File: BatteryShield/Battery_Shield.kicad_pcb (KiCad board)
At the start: 2 copper layers, 95 x 123.4 mm, 66 parts, among them J100 Conn_02x02_Counter_Clockwise, J600 Conn_02x03_Counter_Clockwise, J700 MOLEX-MINIFIT-JR-5556, K100 G5LE-14 DC3, K101 G5LE-14 DC3, K200 G5LE-14 DC3, Q100 ZVP4525G, Q101 ZVP4525G, Q200 ZVP4525G, U300 LTC4151IMS-1, U301 MOCD207M, U302 MOCD207M, U400 ADC081C021, U401 LM35-D, U600 LT8608, U601 LTC3642-3.3

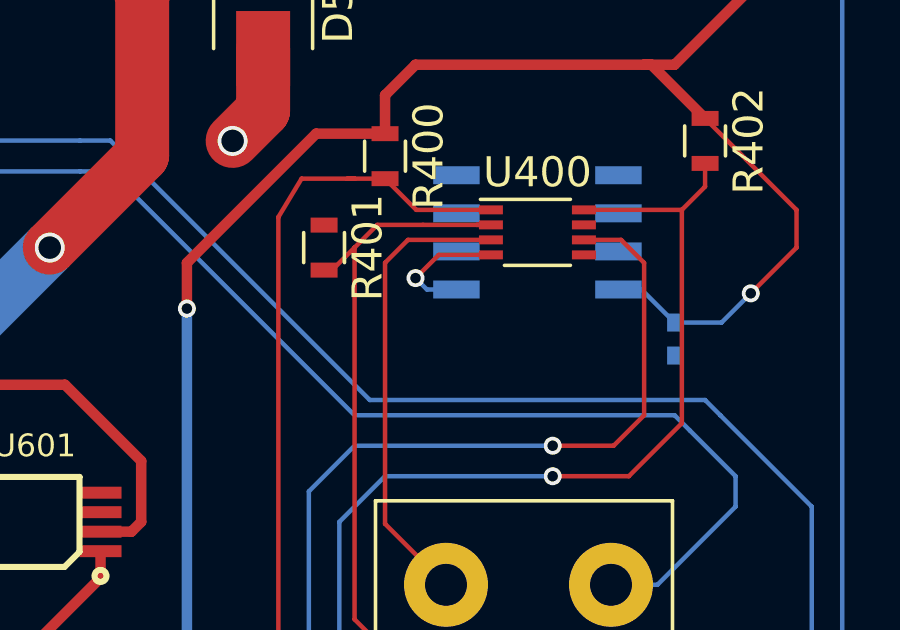
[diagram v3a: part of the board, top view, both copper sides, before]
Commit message: Added minor changes to bom/temp sensor circuit
Added small decoupling cap on temp sensor/adc input. Also added more files to the verifcation document folder
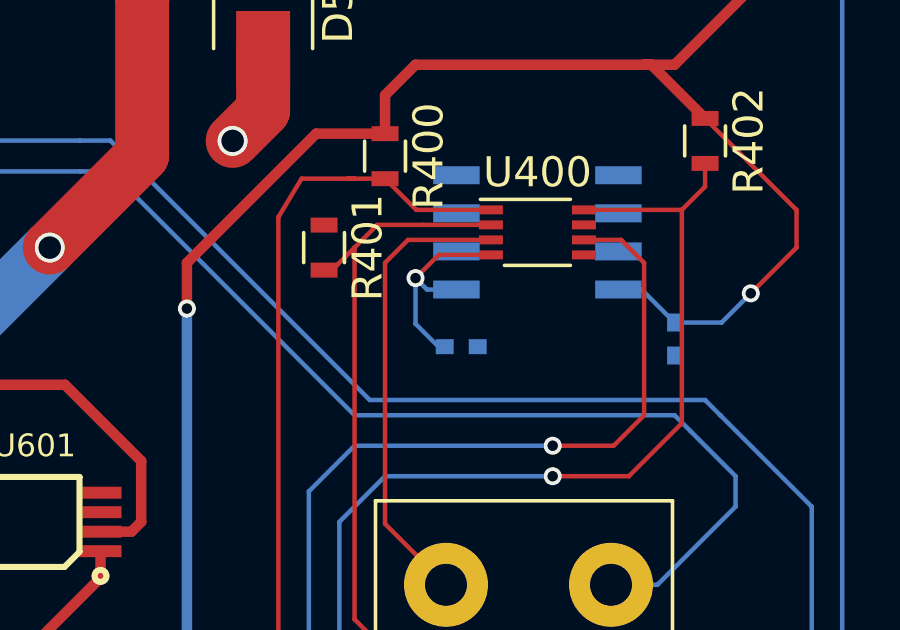
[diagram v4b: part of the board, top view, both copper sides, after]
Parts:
- added C401: 10n, Capacitors_SMD:C_0402, B.Cu at (152.4, 105.4)
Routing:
- net Net-(C401-Pad1): track 4.36 -> 7.17 mm
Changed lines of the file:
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@@
 (kicad_pcb (version 4) (host pcbnew 4.0.7)
   (general
-    (links 149)
+    (links 151)
     (no_connects 13)
     (area 81.712999 36.500999 176.859001 160.095001)
     (thickness 1.6)
     (drawings 5)
-    (tracks 581)
+    (tracks 584)
     (zones 0)
-    (modules 66)
+    (modules 67)
     (nets 53)
   )
@@
   (net 39 "Net-(U302-Pad5)")
   (net 40 "Net-(U302-Pad6)")
-  (net 41 "Net-(U400-Pad4)")
-  (net 42 "Net-(U401-Pad2)")
-  (net 43 "Net-(U401-Pad3)")
-  (net 44 "Net-(U401-Pad5)")
-  (net 45 "Net-(U401-Pad6)")
-  (net 46 "Net-(U401-Pad7)")
-  (net 47 "Net-(U601-Pad3)")
-  (net 48 "Net-(U601-Pad4)")
-  (net 49 "Net-(U601-Pad7)")
-  (net 50 "Net-(L600-Pad2)")
-  (net 51 "Net-(U600-Pad7)")
-  (net 52 "Net-(U600-Pad8)")
+  (net 41 "Net-(U401-Pad2)")
+  (net 42 "Net-(U401-Pad3)")
+  (net 43 "Net-(U401-Pad5)")
+  (net 44 "Net-(U401-Pad6)")
+  (net 45 "Net-(U401-Pad7)")
+  (net 46 "Net-(U601-Pad3)")
+  (net 47 "Net-(U601-Pad4)")
+  (net 48 "Net-(U601-Pad7)")
+  (net 49 "Net-(L600-Pad2)")
+  (net 50 "Net-(U600-Pad7)")
+  (net 51 "Net-(U600-Pad8)")
+  (net 52 "Net-(C401-Pad1)")
   (net_class Default "This is the default net class."
     (clearance 0.15)
@@
     (add_net CV_SCL_BBB)
     (add_net CV_SDA_BBB)
+    (add_net "Net-(C401-Pad1)")
     (add_net "Net-(C601-Pad1)")
     (add_net "Net-(C601-Pad2)")
@@
     (add_net "Net-(U302-Pad5)")
     (add_net "Net-(U302-Pad6)")
-    (add_net "Net-(U400-Pad4)")
     (add_net "Net-(U401-Pad2)")
     (add_net "Net-(U401-Pad3)")
@@
       (net 18 5V_REG))
     (pad 2 smd rect (at 2.44 0 90) (size 1.6 3.5) (layers F.Cu F.Paste F.Mask)
-      (net 50 "Net-(L600-Pad2)"))
+      (net 49 "Net-(L600-Pad2)"))
     (model ${KISYS3DMOD}/Inductors_SMD.3dshapes/L_1812.wrl
       (at (xyz 0 0 0))
@@
     (fp_line (start -2.075 2.525) (end -3.475 2.525) (layer B.SilkS) (width 0.15))
     (pad 1 smd rect (at -2.7 1.905) (size 1.55 0.6) (layers B.Cu B.Paste B.Mask)
-      (net 41 "Net-(U400-Pad4)"))
+      (net 52 "Net-(C401-Pad1)"))
     (pad 2 smd rect (at -2.7 0.635) (size 1.55 0.6) (layers B.Cu B.Paste B.Mask)
-      (net 42 "Net-(U401-Pad2)"))
+      (net 41 "Net-(U401-Pad2)"))
     (pad 3 smd rect (at -2.7 -0.635) (size 1.55 0.6) (layers B.Cu B.Paste B.Mask)
-      (net 43 "Net-(U401-Pad3)"))
+      (net 42 "Net-(U401-Pad3)"))
     (pad 4 smd rect (at -2.7 -1.905) (size 1.55 0.6) (layers B.Cu B.Paste B.Mask)
       (net 1 BBB_GND))
     (pad 5 smd rect (at 2.7 -1.905) (size 1.55 0.6) (layers B.Cu B.Paste B.Mask)
-      (net 44 "Net-(U401-Pad5)"))
+      (net 43 "Net-(U401-Pad5)"))
     (pad 6 smd rect (at 2.7 -0.635) (size 1.55 0.6) (layers B.Cu B.Paste B.Mask)
-      (net 45 "Net-(U401-Pad6)"))
+      (net 44 "Net-(U401-Pad6)"))
     (pad 7 smd rect (at 2.7 0.635) (size 1.55 0.6) (layers B.Cu B.Paste B.Mask)
-      (net 46 "Net-(U401-Pad7)"))
+      (net 45 "Net-(U401-Pad7)"))
     (pad 8 smd rect (at 2.7 1.905) (size 1.55 0.6) (layers B.Cu B.Paste B.Mask)
       (net 18 5V_REG))
@@
       (net 3 V_BATT37))
     (pad 3 smd rect (at -2.2 0.325 180) (size 1.4 0.4) (layers F.Cu F.Paste F.SilkS F.Mask)
-      (net 47 "Net-(U601-Pad3)"))
+      (net 46 "Net-(U601-Pad3)"))
     (pad 4 smd rect (at -2.2 0.975 180) (size 1.4 0.4) (layers F.Cu F.Paste F.SilkS F.Mask)
-      (net 48 "Net-(U601-Pad4)"))
+      (net 47 "Net-(U601-Pad4)"))
     (pad 5 smd rect (at 2.2 0.975 180) (size 1.4 0.4) (layers F.Cu F.Paste F.SilkS F.Mask)
       (net 3 V_BATT37))
@@
       (net 8 3.3V_REG))
     (pad 7 smd rect (at 2.2 -0.325 180) (size 1.4 0.4) (layers F.Cu F.Paste F.SilkS F.Mask)
-      (net 49 "Net-(U601-Pad7)"))
+      (net 48 "Net-(U601-Pad7)"))
     (pad 8 smd rect (at 2.2 -0.975 180) (size 1.4 0.4) (layers F.Cu F.Paste F.SilkS F.Mask)
       (net 1 BBB_GND))
@@
       (net 25 TEMP_SLAVE_ADDR0))
     (pad 4 smd rect (at -1.55 0.75 270) (size 0.3 0.8) (layers F.Cu F.Paste F.Mask)
-      (net 41 "Net-(U400-Pad4)"))
+      (net 52 "Net-(C401-Pad1)"))
     (pad 5 smd rect (at 1.55 0.75 270) (size 0.3 0.8) (layers F.Cu F.Paste F.Mask)
       (net 18 5V_REG))
@@
       (net 6 "Net-(C602-Pad1)"))
     (pad 2 smd rect (at -2.2 -0.5 90) (size 1.6 0.3) (layers F.Cu F.Paste F.SilkS F.Mask)
-      (net 50 "Net-(L600-Pad2)"))
+      (net 49 "Net-(L600-Pad2)"))
     (pad 3 smd rect (at -2.2 0 90) (size 1.6 0.3) (layers F.Cu F.Paste F.SilkS F.Mask)
       (net 5 "Net-(C601-Pad1)"))
@@
       (net 7 "Net-(C603-Pad2)"))
     (pad 7 smd rect (at 2.2 0.5 90) (size 1.6 0.3) (layers F.Cu F.Paste F.SilkS F.Mask)
-      (net 51 "Net-(U600-Pad7)"))
+      (net 50 "Net-(U600-Pad7)"))
     (pad 8 smd rect (at 2.2 0 90) (size 1.6 0.3) (layers F.Cu F.Paste F.SilkS F.Mask)
-      (net 52 "Net-(U600-Pad8)"))
+      (net 51 "Net-(U600-Pad8)"))
     (pad 9 smd rect (at 2.2 -0.5 90) (size 1.6 0.3) (layers F.Cu F.Paste F.SilkS F.Mask)
       (net 3 V_BATT37))
@@
       (net 1 BBB_GND))
   )
+  (module Capacitors_SMD:C_0402 (layer B.Cu)
+    (at 152.4 105.41)
+    (descr "Capacitor SMD 0402, reflow soldering, AVX (see smccp.pdf)")
+    (tags "capacitor 0402")
+    (attr smd)
+    (fp_text reference C401 (at 0 1.27) (layer B.SilkS)
+      (effects (font (size 1 1) (thickness 0.15)) (justify mirror))
+    )
+    (fp_text value 10n (at 0 -1.27) (layer B.Fab)
+      (effects (font (size 1 1) (thickness 0.15)) (justify mirror))
+    )
+    (fp_text user %R (at 0 1.27) (layer B.Fab)
+      (effects (font (size 1 1) (thickness 0.15)) (justify mirror))
+    )
+    (fp_line (start -0.5 -0.25) (end -0.5 0.25) (layer B.Fab) (width 0.1))
+    (fp_line (start 0.5 -0.25) (end -0.5 -0.25) (layer B.Fab) (width 0.1))
+    (fp_line (start 0.5 0.25) (end 0.5 -0.25) (layer B.Fab) (width 0.1))
+    (fp_line (start -0.5 0.25) (end 0.5 0.25) (layer B.Fab) (width 0.1))
+    (fp_line (start 0.25 0.47) (end -0.25 0.47) (layer B.SilkS) (width 0.12))
+    (fp_line (start -0.25 -0.47) (end 0.25 -0.47) (layer B.SilkS) (width 0.12))
+    (fp_line (start -1 0.4) (end 1 0.4) (layer B.CrtYd) (width 0.05))
+    (fp_line (start -1 0.4) (end -1 -0.4) (layer B.CrtYd) (width 0.05))
+    (fp_line (start 1 -0.4) (end 1 0.4) (layer B.CrtYd) (width 0.05))
+    (fp_line (start 1 -0.4) (end -1 -0.4) (layer B.CrtYd) (width 0.05))
+    (pad 1 smd rect (at -0.55 0) (size 0.6 0.5) (layers B.Cu B.Paste B.Mask)
+      (net 52 "Net-(C401-Pad1)"))
+    (pad 2 smd rect (at 0.55 0) (size 0.6 0.5) (layers B.Cu B.Paste B.Mask)
+      (net 1 BBB_GND))
+    (model Capacitors_SMD.3dshapes/C_0402.wrl
+      (at (xyz 0 0 0))
+      (scale (xyz 1 1 1))
+      (rotate (xyz 0 0 0))
+    )
+  )
   (gr_line (start 176.784 36.576) (end 128.524 36.576) (angle 90) (layer Edge.Cuts) (width 0.15))
   (gr_line (start 176.784 160.02) (end 176.784 36.576) (angle 90) (layer Edge.Cuts) (width 0.15))
@@
   (segment (start 125.476 112.776) (end 127.266 110.986) (width 0.15) (layer F.Cu) (net 36))
   (segment (start 127.508 110.478) (end 127.266 110.236) (width 0.15) (layer F.Cu) (net 36))
-  (segment (start 152.24 103.505) (end 151.257 103.505) (width 0.15) (layer B.Cu) (net 41))
-  (segment (start 151.65 102.35) (end 153.39 102.35) (width 0.15) (layer F.Cu) (net 41))
-  (segment (start 150.876 103.124) (end 151.65 102.35) (width 0.15) (layer F.Cu) (net 41))
-  (via (at 150.876 103.124) (size 0.6) (drill 0.35) (layers F.Cu B.Cu) (net 41))
-  (segment (start 151.257 103.505) (end 150.876 103.124) (width 0.15) (layer B.Cu) (net 41))
-  (segment (start 121.42 119.548) (end 121.42 120.488) (width 0.35) (layer F.Cu) (net 50))
-  (segment (start 121.42 120.488) (end 118.872 123.036) (width 0.35) (layer F.Cu) (net 50))
-  (segment (start 122.42 114.308) (end 122.42 115.148) (width 0.15) (layer F.Cu) (net 51) (status 20))
-  (segment (start 122.42 115.656) (end 122.42 115.324) (width 0.15) (layer F.Cu) (net 51) (status 30))
-  (segment (start 121.92 115.656) (end 121.92 115.316) (width 0.15) (layer F.Cu) (net 52) (status 30))
+  (segment (start 121.42 119.548) (end 121.42 120.488) (width 0.35) (layer F.Cu) (net 49))
+  (segment (start 121.42 120.488) (end 118.872 123.036) (width 0.35) (layer F.Cu) (net 49))
+  (segment (start 122.42 114.308) (end 122.42 115.148) (width 0.15) (layer F.Cu) (net 50) (status 20))
+  (segment (start 122.42 115.656) (end 122.42 115.324) (width 0.15) (layer F.Cu) (net 50) (status 30))
+  (segment (start 121.92 115.656) (end 121.92 115.316) (width 0.15) (layer F.Cu) (net 51) (status 30))
+  (segment (start 151.85 105.41) (end 151.638 105.41) (width 0.15) (layer B.Cu) (net 52) (status C00000))
+  (segment (start 151.638 105.41) (end 150.876 104.648) (width 0.15) (layer B.Cu) (net 52) (status 400000))
+  (segment (start 150.876 104.648) (end 150.876 103.124) (width 0.15) (layer B.Cu) (net 52))
+  (segment (start 152.24 103.505) (end 151.257 103.505) (width 0.15) (layer B.Cu) (net 52))
+  (segment (start 151.65 102.35) (end 153.39 102.35) (width 0.15) (layer F.Cu) (net 52))
+  (segment (start 150.876 103.124) (end 151.65 102.35) (width 0.15) (layer F.Cu) (net 52))
+  (via (at 150.876 103.124) (size 0.6) (drill 0.35) (layers F.Cu B.Cu) (net 52))
+  (segment (start 151.257 103.505) (end 150.876 103.124) (width 0.15) (layer B.Cu) (net 52))
   (zone (net 1) (net_name BBB_GND) (layer B.Cu) (hatch edge 0.508)
     (connect_pads (clearance 0.508))

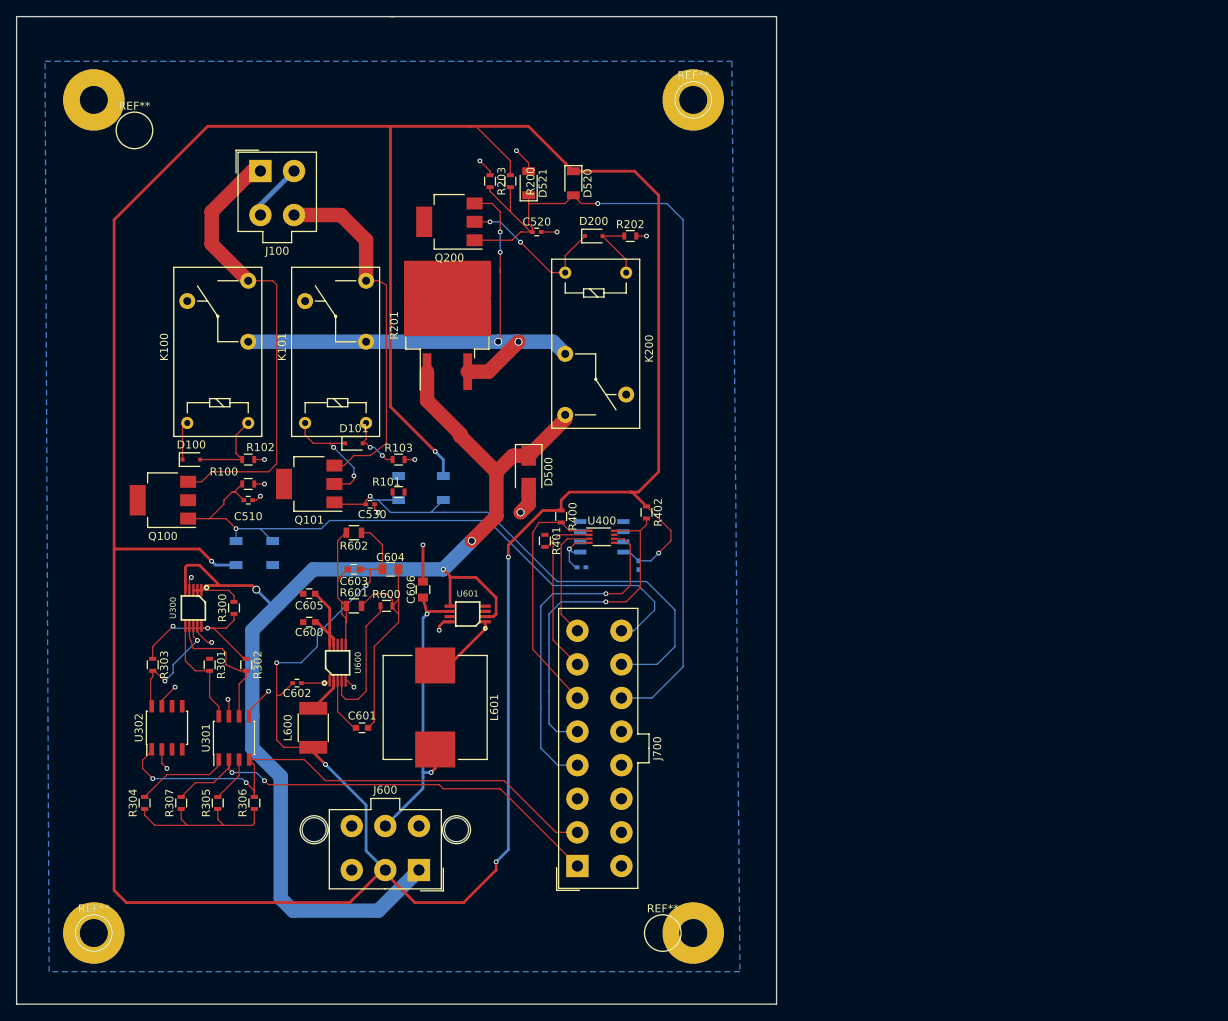
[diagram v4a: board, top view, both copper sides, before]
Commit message: Changed BBB regulation voltage from 5V to 3.3V
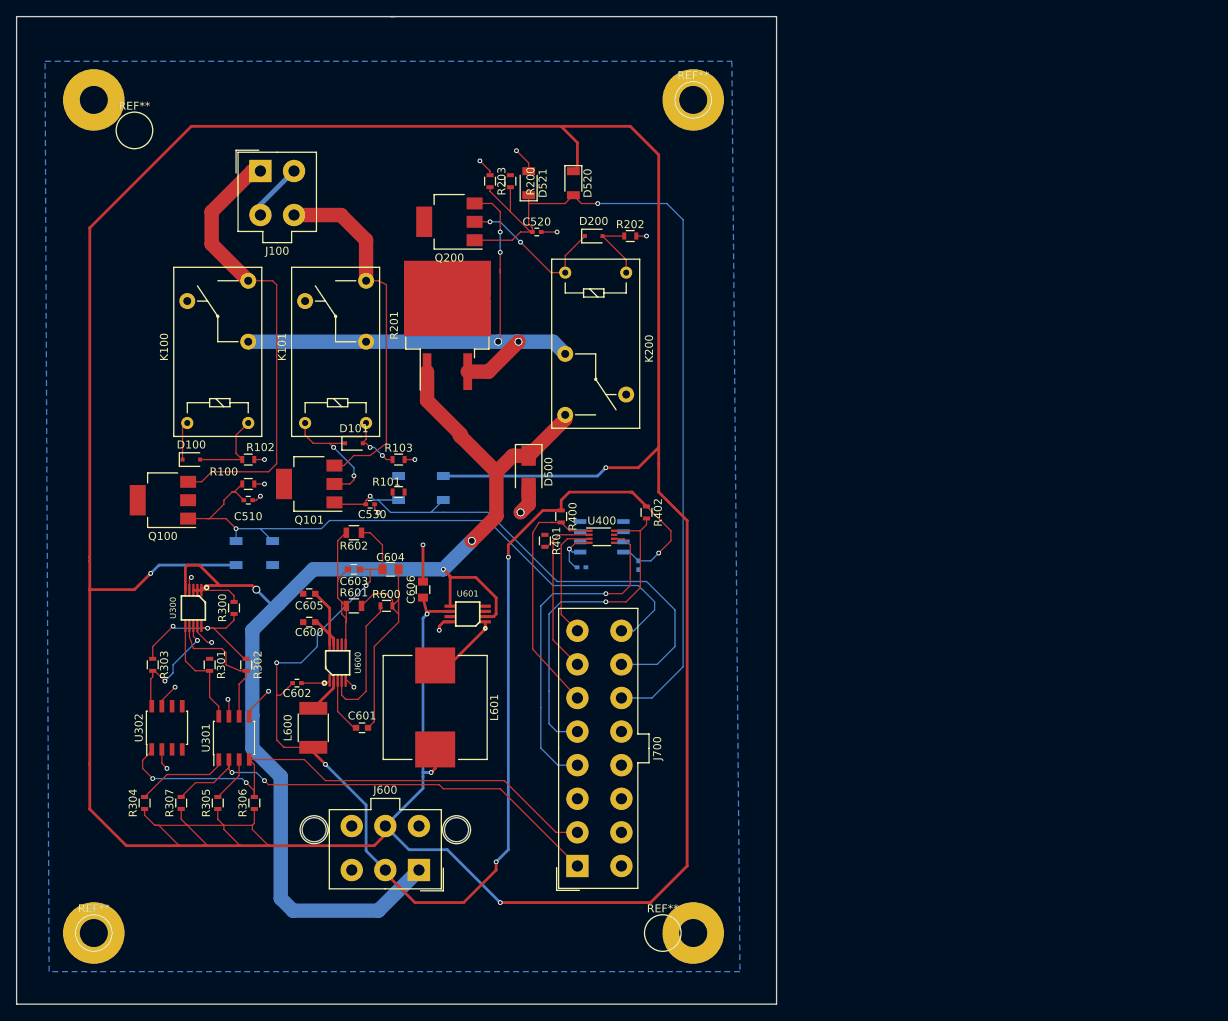
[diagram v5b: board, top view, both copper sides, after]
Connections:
- D510 pad 1: 5V_REG -> 3.3V_REG
- D520 pad 1: 5V_REG -> 3.3V_REG
- D530 pad 1: 5V_REG -> 3.3V_REG
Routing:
- net 3.3V_REG: track 59.3 -> 453.8 mm, vias 2 -> 5
- net 5V_REG: track 466.7 -> 160.2 mm, vias 8 -> 6

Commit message: Redid Layout for battery shield. Now V2
Way cleaner, no trace loops and the ground plane is MUCH cleaner.
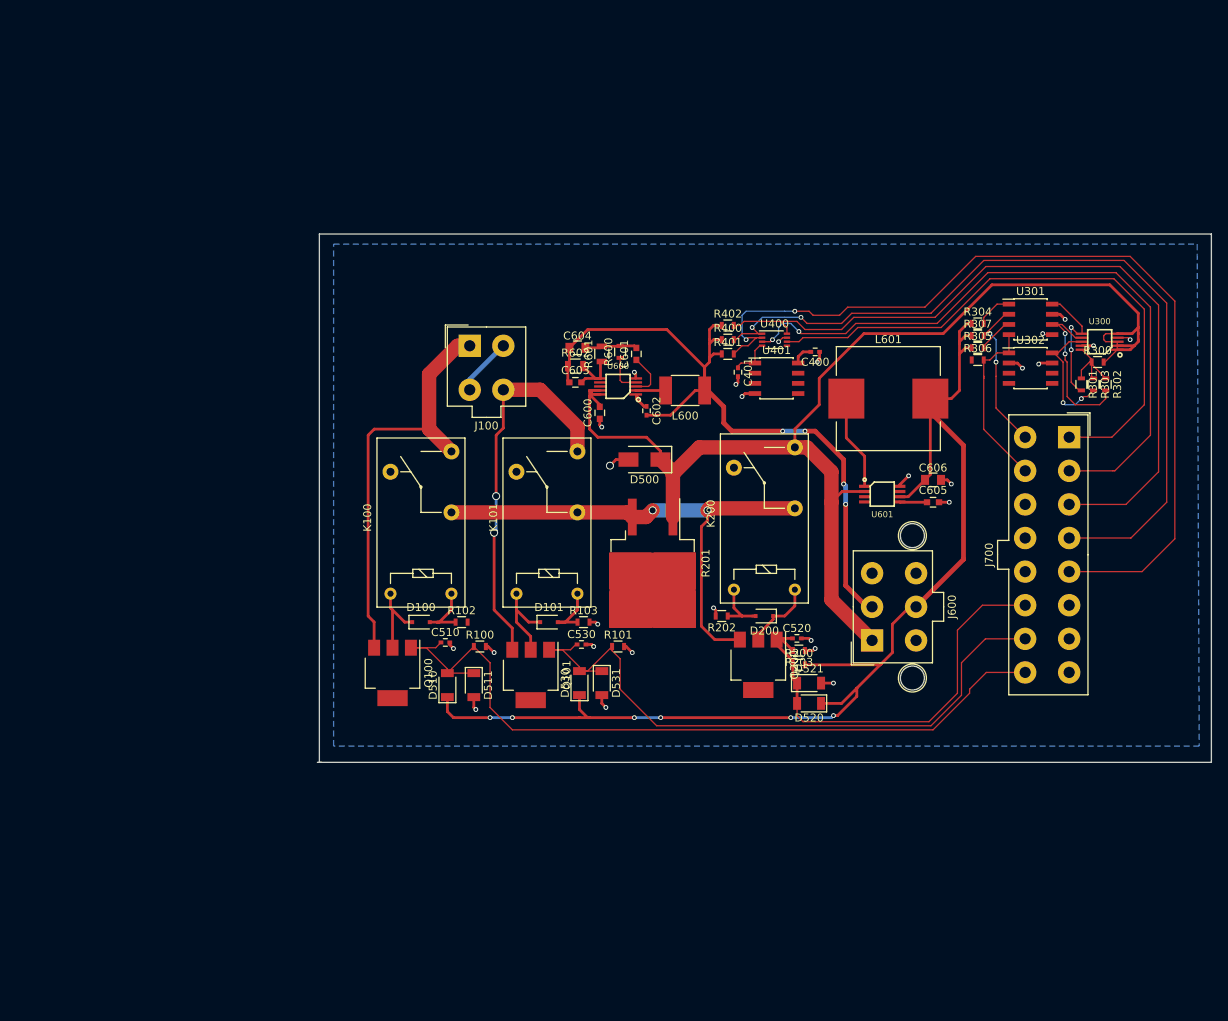
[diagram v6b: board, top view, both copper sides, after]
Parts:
- removed G***: LOGO, footprints:logoSmall
- removed REF** (x4): 1pin, Connectors:1pin
- C400, C401, D510, D511, D530, D531, U401: moved to F.Cu
- moved R303 122.7 mm to (216.4, 82.5)
- moved R304 120.2 mm to (201.9, 74.9), turned to 0 degrees
- moved U300 118.1 mm to (217.2, 77.2), turned to 180 degrees
- moved U302 116.9 mm to (208.5, 80.5), turned to 0 degrees
- moved R307 115.4 mm to (201.9, 76.5), turned to 0 degrees
- moved R301 114.5 mm to (214.9, 82.5)
- moved R302 113.0 mm to (217.9, 82.5)
- moved U301 112.5 mm to (208.5, 74.4), turned to 0 degrees
- moved R300 112.2 mm to (216.9, 79.8), turned to 0 degrees
- moved R305 110.7 mm to (201.9, 78.0), turned to 0 degrees
- moved R306 106.0 mm to (201.9, 79.5), turned to 0 degrees
- moved J700 81.6 mm to (213.4, 89.2), turned to 270 degrees
- moved C605 78.8 mm to (196.3, 97.3), turned to 0 degrees
- moved D521 71.6 mm to (180.8, 119.9), turned to 0 degrees
- moved D520 71.4 mm to (180.8, 122.4), turned to 180 degrees
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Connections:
- J700 pad 1: CV_SCL_BBB -> TEMP_SLAVE_ADDR1
- J700 pad 10: BBB_GND -> CV_SDA_BBB
- J700 pad 2: CV_SDA_BBB -> TEMP_SLAVE_ADDR0
- J700 pad 3: BBB_GND -> TEMP_SDA_BBB
- J700 pad 4: TEMP_SLAVE_ADDR1 -> TEMP_SCL_BBB
- J700 pad 5: TEMP_SDA_BBB -> TEMP_DIN_BBB
- J700 pad 6: TEMP_SCL_BBB -> BBB_GND
- J700 pad 7: TEMP_DIN_BBB -> BBB_GND
- J700 pad 8: TEMP_SLAVE_ADDR0 -> BBB_GND
- J700 pad 9: BBB_GND -> CV_SCL_BBB
- R200 pad 2: 5V_REG -> 3.3V_REG
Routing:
- net 3.3V_REG: track 453.8 -> 149.5 mm, vias 5 -> 6
- net TEMP_DIN_BBB: track 23.4 -> 114.0 mm, vias 0 -> 2
- net TEMP_SCL_BBB: track 31.3 -> 102.5 mm, vias 0 -> 2
- net TEMP_SLAVE_ADDR0: track 15.4 -> 83.4 mm, vias 0 -> 2
- net 5V_REG: track 160.2 -> 94.5 mm, vias 6 -> 4
- net PRECHARGE_N: track 109.6 -> 54.7 mm, vias 1 -> 0
- net TEMP_SDA_BBB: track 42.7 -> 94.5 mm, vias 1 -> 0
- net CV_SDA_BBB: track 68.1 -> 22.1 mm, vias 2 -> 0
- net CV_SCL_BBB: track 58.8 -> 19.4 mm
- net TEMP_SLAVE_ADDR1: track 42.9 -> 72.5 mm, vias 1 -> 0
- net Net-(C601-Pad2): track 30.5 -> 6.66 mm
- net V_BATT37: track 179.3 -> 157.7 mm, vias 3 -> 0
- net PACK_A_ON_N: track 81.8 -> 98.0 mm, vias 1 -> 0
- net PACK_B_ON_N: track 66.2 -> 82.3 mm, vias 1 -> 0
- net Net-(C603-Pad2): track 20.3 -> 7.59 mm
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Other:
- board size 95 x 123.4 mm -> 111.8 x 66 mm
